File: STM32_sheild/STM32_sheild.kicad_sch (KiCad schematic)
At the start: 51 parts, among them J1 61612002121503, J2 CN7, J3 CN10, J4 632722100213, J5 691210910002, J6 691210910002, U1 OPA333xxDBV, U2 TPS63031DSK, U3 MCP73831-2-MC, U4 OPA333xxDBV

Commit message: Changes to layout
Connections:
- net GND: now also D4.1 (A1); no longer D4.2 (A2)
- net OPA_IN+: no longer D4.1 (A1), R11.2, U4.3 (+)
- net OPA_IN-: no longer R12.1, R13.1, U4.4 (-)
- net OPA_VDD: no longer C10.1, C11.1, R15.1, U4.5 (V+)
- net OPA_out: no longer R13.2, R14.1, U4.1
- new net OPA2_IN+: D4.2 (A2), R11.2, U4.3 (+)
- new net OPA2_IN-: R12.1, R13.1, U4.4 (-)
- new net OPA2_VDD: C10.1, C11.1, R15.1, U4.5 (V+)
- new net OPA2_out: R13.2, R14.1, U4.1
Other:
- moved on the sheet: D4
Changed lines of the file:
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@@
 	)
 	(junction
-		(at 77.47 106.68)
-		(diameter 0)
-		(color 0 0 0 0)
-	)
-	(junction
 		(at 92.71 205.74)
 		(diameter 0)
@@
 	)
 	(junction
+		(at 77.47 106.68)
+		(diameter 0)
+		(color 0 0 0 0)
+	)
+	(junction
 		(at 175.26 212.09)
 		(diameter 0)
@@
 	(wire
 		(pts
-			(xy 77.47 106.68) (xy 100.33 106.68)
-		)
-		(stroke
-			(width 0)
-			(type default)
-		)
-	)
-	(wire
-		(pts
 			(xy 288.29 45.72) (xy 265.43 45.72)
 		)
@@
 	(wire
 		(pts
+			(xy 73.66 106.68) (xy 77.47 106.68)
+		)
+		(stroke
+			(width 0)
+			(type default)
+		)
+	)
+	(wire
+		(pts
 			(xy 156.21 80.01) (xy 156.21 82.55)
 		)
@@
 	(wire
 		(pts
+			(xy 77.47 106.68) (xy 100.33 106.68)
+		)
+		(stroke
+			(width 0)
+			(type default)
+		)
+	)
+	(wire
+		(pts
 			(xy 240.03 204.47) (xy 240.03 207.01)
 		)
@@
 	(wire
 		(pts
-			(xy 73.66 106.68) (xy 77.47 106.68)
-		)
-		(stroke
-			(width 0)
-			(type default)
-		)
-	)
-	(wire
-		(pts
 			(xy 113.03 86.36) (xy 113.03 88.9)
 		)
@@
 		)
 	)
-	(label "OPA_VDD"
+	(label "OPA2_VDD"
 		(at 105.41 86.36 0)
 		(effects
@@
 		)
 	)
-	(label "OPA_IN-"
+	(label "OPA2_IN-"
 		(at 91.44 111.76 0)
 		(effects
@@
 		)
 	)
-	(label "OPA_out"
+	(label "OPA2_out"
 		(at 115.57 109.22 0)
 		(effects
@@
 		)
 	)
-	(label "OPA_IN+"
+	(label "OPA2_IN+"
 		(at 91.44 106.68 0)
 		(effects
@@
 	(symbol
 		(lib_id "Diode:ESD9B3.3ST5G")
-		(at 77.47 110.49 270)
+		(at 77.47 110.49 90)
 		(unit 1)
 		(body_style 1)
@@
 		(dnp no)
 		(property "Reference" "D4"
-			(at 80.01 109.2199 90)
+			(at 81.026 112.776 90)
 			(show_name no)
 			(do_not_autoplace no)
@@
 		)
 		(property "Value" "ESD9B3.3ST5G"
-			(at 81.788 111.252 0)
+			(at 73.914 122.682 0)
 			(show_name no)
 			(do_not_autoplace no)
@@
 	(group "3.3V reg"
 		(members "012e8882-bec8-4df7-99f7-49c5f0b348d8" "04a5907e-48fe-419a-b4f0-6bcfc45b3919"
-			"0a47bc87-bd80-4b06-841a-d5804b13685b" "0a649811-39c2-4c22-a7ce-e8bf44e1fe1b"
-			"0dfc2b48-0e6b-4dcd-9009-62f3c65e5019" "0e397cc8-8699-457f-a2e7-6c54b7d52372"
-			"1c97f8c0-bb12-48e2-8f49-c6c66ff1a33f" "1e27f09a-9b31-47e4-84c5-f4d15a95a9cc"
-			"1e530a42-bf31-4c07-a453-18824bf5bc5d" "22f87fbf-b579-41a1-b6d0-d61e432bdf4a"
-			"352cdb50-3d76-4e93-9cf2-ddae7d39770f" "37397ab8-0242-4038-b218-159c4452d13f"
-			"415b9213-bd82-4131-a540-2b643ab24f0f" "44b93b55-1e7e-4917-ae03-c703a69a4314"
-			"54cd264f-715c-468f-93ca-3c22021cd22a" "5be8eb28-d0a8-4c82-b155-63c0ddfcf6d2"
-			"6320a3fa-2ae3-4858-8356-5ab1419474cb" "66c1d99b-3674-4c45-9ef8-168f34758e6a"
-			"6fbee214-e075-4960-b9a8-589303b214ef" "70f298f4-0582-428a-8561-1f4f00130a07"
-			"78f1e04a-dbe6-464f-bb99-a0da3b7b66ed" "7a1a7a43-f5fa-41a3-bdf2-7d86a0433427"
-			"7a56ee4f-7b94-491a-854a-71998465a41d" "81edab79-51aa-4a2b-b27f-13d633822b9b"
-			"85d7222c-d5c5-41ba-9f41-b19f82ed3bdb" "883dda52-ef7c-4cb4-b8ba-b8c31b2888ba"
-			"9928c836-67fa-479a-a340-e9b1543938d5" "9962f244-1e5b-46f2-b775-dc115eb1df32"
-			"9e4300a6-d1d7-4cb7-8960-58e61cf219da" "a1df7d2d-1770-497e-9e5c-08a5c94d42b7"
-			"a2dd8dd1-5921-453f-9e48-35f70f94815a" "a32a1507-538c-4481-bcda-0fdbe5f3747f"
-			"aeede997-53b1-49fb-8457-1023b4b5990a" "b5b3e238-842f-48ca-b330-50807502f6b7"
-			"b5b74a64-f55f-4db1-b190-e4c6ab60eff4" "b67b7ed1-aea8-4afb-857d-b22b1727eeb2"
-			"b7bee332-4483-4e25-be0f-c3a3e0335a1a" "c2ffda40-90d0-4961-aea3-13d1b22963e6"
-			"c593caa9-0e7c-4825-af24-d51c7b418972" "c9175dbe-748e-4f3f-b695-7b213e84d62a"
-			"cdff2a33-3029-4b8e-a4b0-37a910e59040" "d1bb574c-cd3c-449e-83e3-980af346770d"
-			"d39192f8-19a0-43ea-a1b2-0c417f7bae17" "d8b329e0-7080-4335-857b-910e9e0aee89"
-			"d90145f0-9243-4f36-ad26-269a51702e4a" "dffb99d8-4214-4ce9-a9ad-6b8b8e2a4a35"
-			"ec840ac7-fd87-4c7a-8506-b3157a9104ed" "f182ab6e-92d0-4a33-b374-119a35620c30"
-			"f8f6e554-9eaf-4c3b-85e9-c57b11652fed" "fa8cbebf-1487-40d9-bb6f-aa7969012d48"
-			"ff6abb2f-123b-437d-854a-8129c08195af"
+			"0a649811-39c2-4c22-a7ce-e8bf44e1fe1b" "0dfc2b48-0e6b-4dcd-9009-62f3c65e5019"
+			"0e397cc8-8699-457f-a2e7-6c54b7d52372" "1c97f8c0-bb12-48e2-8f49-c6c66ff1a33f"
+			"1e27f09a-9b31-47e4-84c5-f4d15a95a9cc" "1e530a42-bf31-4c07-a453-18824bf5bc5d"
+			"22f87fbf-b579-41a1-b6d0-d61e432bdf4a" "352cdb50-3d76-4e93-9cf2-ddae7d39770f"
+			"37397ab8-0242-4038-b218-159c4452d13f" "415b9213-bd82-4131-a540-2b643ab24f0f"
+			"44b93b55-1e7e-4917-ae03-c703a69a4314" "54cd264f-715c-468f-93ca-3c22021cd22a"
+			"5be8eb28-d0a8-4c82-b155-63c0ddfcf6d2" "6320a3fa-2ae3-4858-8356-5ab1419474cb"
+			"66c1d99b-3674-4c45-9ef8-168f34758e6a" "6fbee214-e075-4960-b9a8-589303b214ef"
+			"70f298f4-0582-428a-8561-1f4f00130a07" "78f1e04a-dbe6-464f-bb99-a0da3b7b66ed"
+			"7a1a7a43-f5fa-41a3-bdf2-7d86a0433427" "7a56ee4f-7b94-491a-854a-71998465a41d"
+			"81edab79-51aa-4a2b-b27f-13d633822b9b" "85d7222c-d5c5-41ba-9f41-b19f82ed3bdb"
+			"883dda52-ef7c-4cb4-b8ba-b8c31b2888ba" "9928c836-67fa-479a-a340-e9b1543938d5"
+			"9962f244-1e5b-46f2-b775-dc115eb1df32" "9e4300a6-d1d7-4cb7-8960-58e61cf219da"
+			"a1df7d2d-1770-497e-9e5c-08a5c94d42b7" "a2dd8dd1-5921-453f-9e48-35f70f94815a"
+			"a32a1507-538c-4481-bcda-0fdbe5f3747f" "aeede997-53b1-49fb-8457-1023b4b5990a"
+			"b5b3e238-842f-48ca-b330-50807502f6b7" "b5b74a64-f55f-4db1-b190-e4c6ab60eff4"
+			"b67b7ed1-aea8-4afb-857d-b22b1727eeb2" "b7bee332-4483-4e25-be0f-c3a3e0335a1a"
+			"c2ffda40-90d0-4961-aea3-13d1b22963e6" "c593caa9-0e7c-4825-af24-d51c7b418972"
+			"c9175dbe-748e-4f3f-b695-7b213e84d62a" "cdff2a33-3029-4b8e-a4b0-37a910e59040"
+			"d1bb574c-cd3c-449e-83e3-980af346770d" "d39192f8-19a0-43ea-a1b2-0c417f7bae17"
+			"d8b329e0-7080-4335-857b-910e9e0aee89" "d90145f0-9243-4f36-ad26-269a51702e4a"
+			"dffb99d8-4214-4ce9-a9ad-6b8b8e2a4a35" "ec840ac7-fd87-4c7a-8506-b3157a9104ed"
+			"f182ab6e-92d0-4a33-b374-119a35620c30" "f8f6e554-9eaf-4c3b-85e9-c57b11652fed"
+			"fa8cbebf-1487-40d9-bb6f-aa7969012d48" "ff6abb2f-123b-437d-854a-8129c08195af"
 		)
 	)

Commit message: small changes to schematic
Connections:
- net +3.3V: no longer JP1.3 (B), JP2.3 (B)
- net +3.3V_REG: now also JP1.3 (B), JP2.3 (B)
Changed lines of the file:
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@@
 			)
 		)
-		(property "Value" "+3.3V"
+		(property "Value" "+3.3V_REG"
 			(at 156.21 74.93 0)
 			(show_name no)
@@
 			)
 		)
-		(property "Value" "+3.3V"
-			(at 156.21 16.51 0)
-			(show_name no)
-			(do_not_autoplace no)
-			(effects
-				(font
-					(size 1.27 1.27)
-				)
-			)
-		)
+		(property "Value" "+3.3V_REG"
+			(at 158.75 20.3199 0)
+			(show_name no)
+			(do_not_autoplace no)
+			(effects
+				(font
+					(size 1.27 1.27)
+				)
+				(justify left)
+			)
+		)

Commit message: update
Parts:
- removed J4: 632722100213, KiCad_wurth_USB-C_PD_connector:632722100213, symbol 632722100213:632722100213
- added J7: 629722010114, Connector_SMD_Wurth:J_Wurth_WR-USB_629722010114, symbol Connector_Wurth_WR-USB:629722010114
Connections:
- net GND: now also J7.A1 (GND), J7.A12 (GND1), J7.B1 (GND3), J7.B12 (GND2), J7.S1 (SHIELD), J7.S2 (SHIELD), J7.S3 (SHIELD), J7.S4 (SHIELD), J7.S5 (SHIELD), J7.S6 (SHIELD)
- net V_USB: now also J7.A4 (VBUS), J7.A9 (VBUS1), J7.B4 (VBUS3), J7.B9 (VBUS2)
- net at R8.1: now also J7.A5 (CC1)
- net at R9.1: now also J7.B5 (CC2)
- no-connect marks 0 -> 6

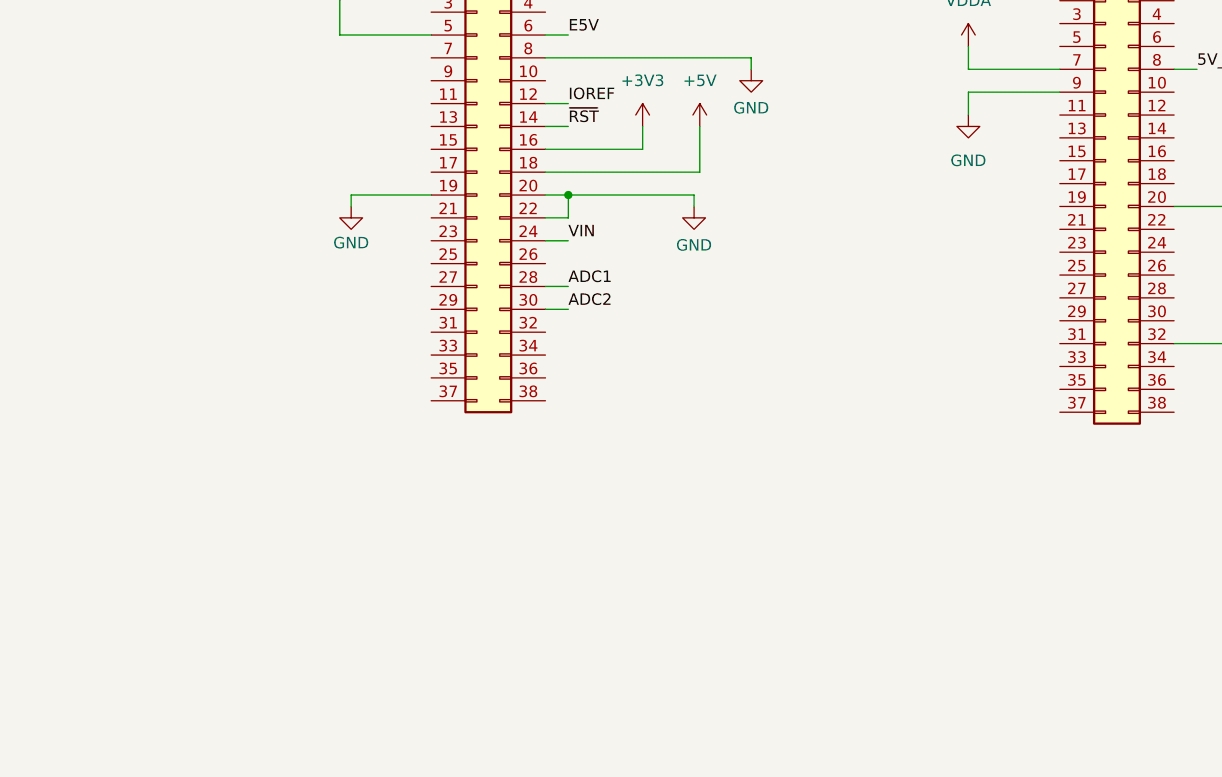
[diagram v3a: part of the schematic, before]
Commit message: added I2C pins
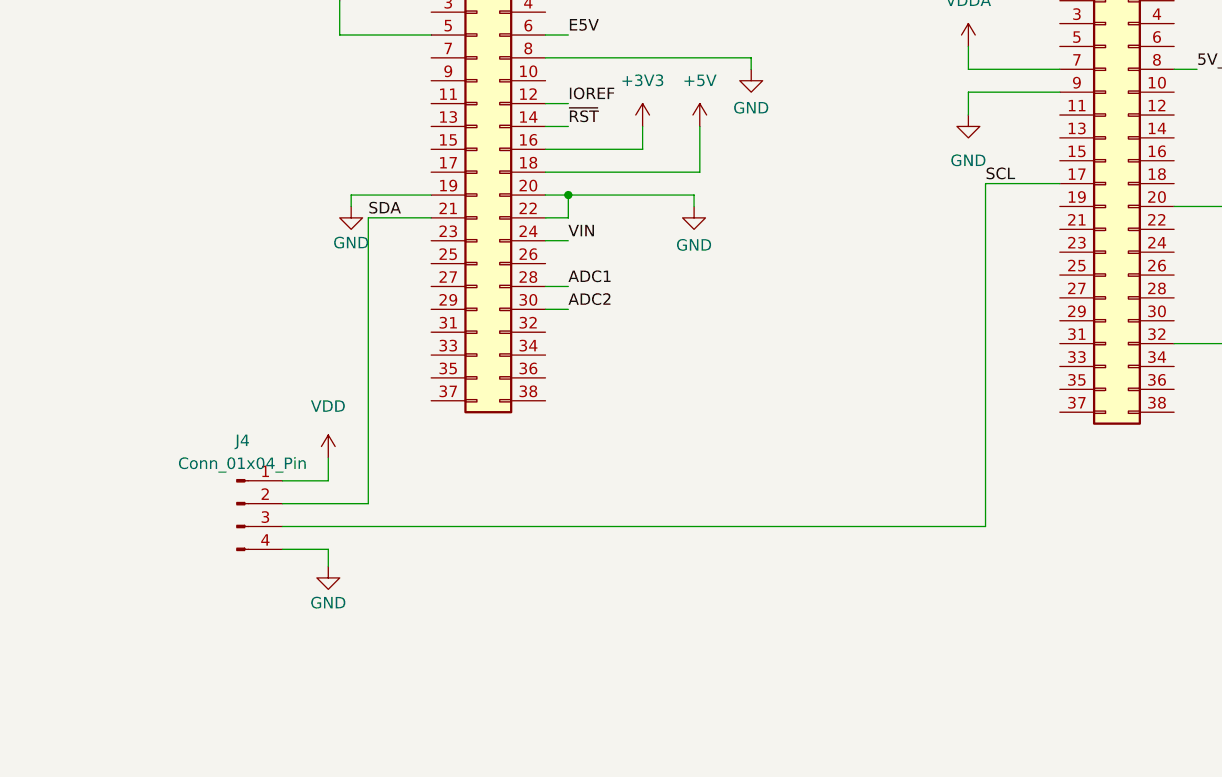
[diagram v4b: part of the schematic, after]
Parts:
- added J4: Conn_01x04_Pin, Connector:FanPinHeader_1x04_P2.54mm_Vertical, symbol Connector:Conn_01x04_Pin
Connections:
- net GND: now also J4.4 (Pin_4)
- net VDD: now also J4.1 (Pin_1)
- net SDA: now reaches J2.21 (Pin_21)
- net SDA: now also J4.2 (Pin_2)
- net SCL: now reaches J3.17 (Pin_17)
- net SCL: now also J4.3 (Pin_3)
